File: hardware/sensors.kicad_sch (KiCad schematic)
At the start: 43 parts, among them U7 PCA9685PW

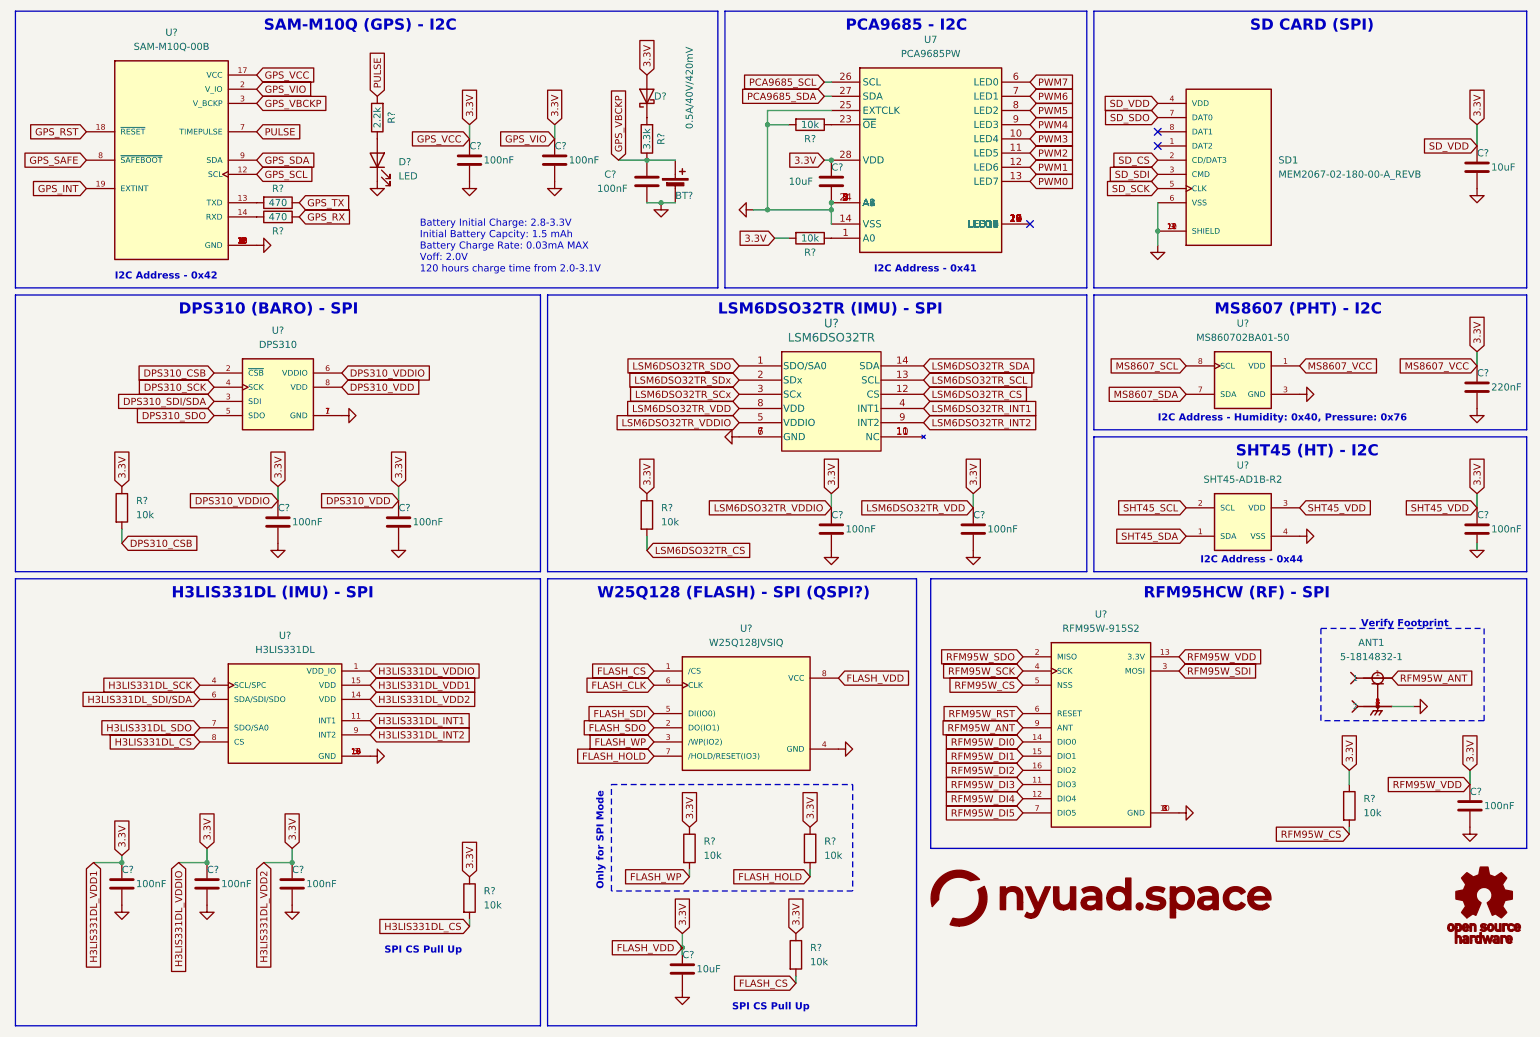
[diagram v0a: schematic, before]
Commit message: added BNO086
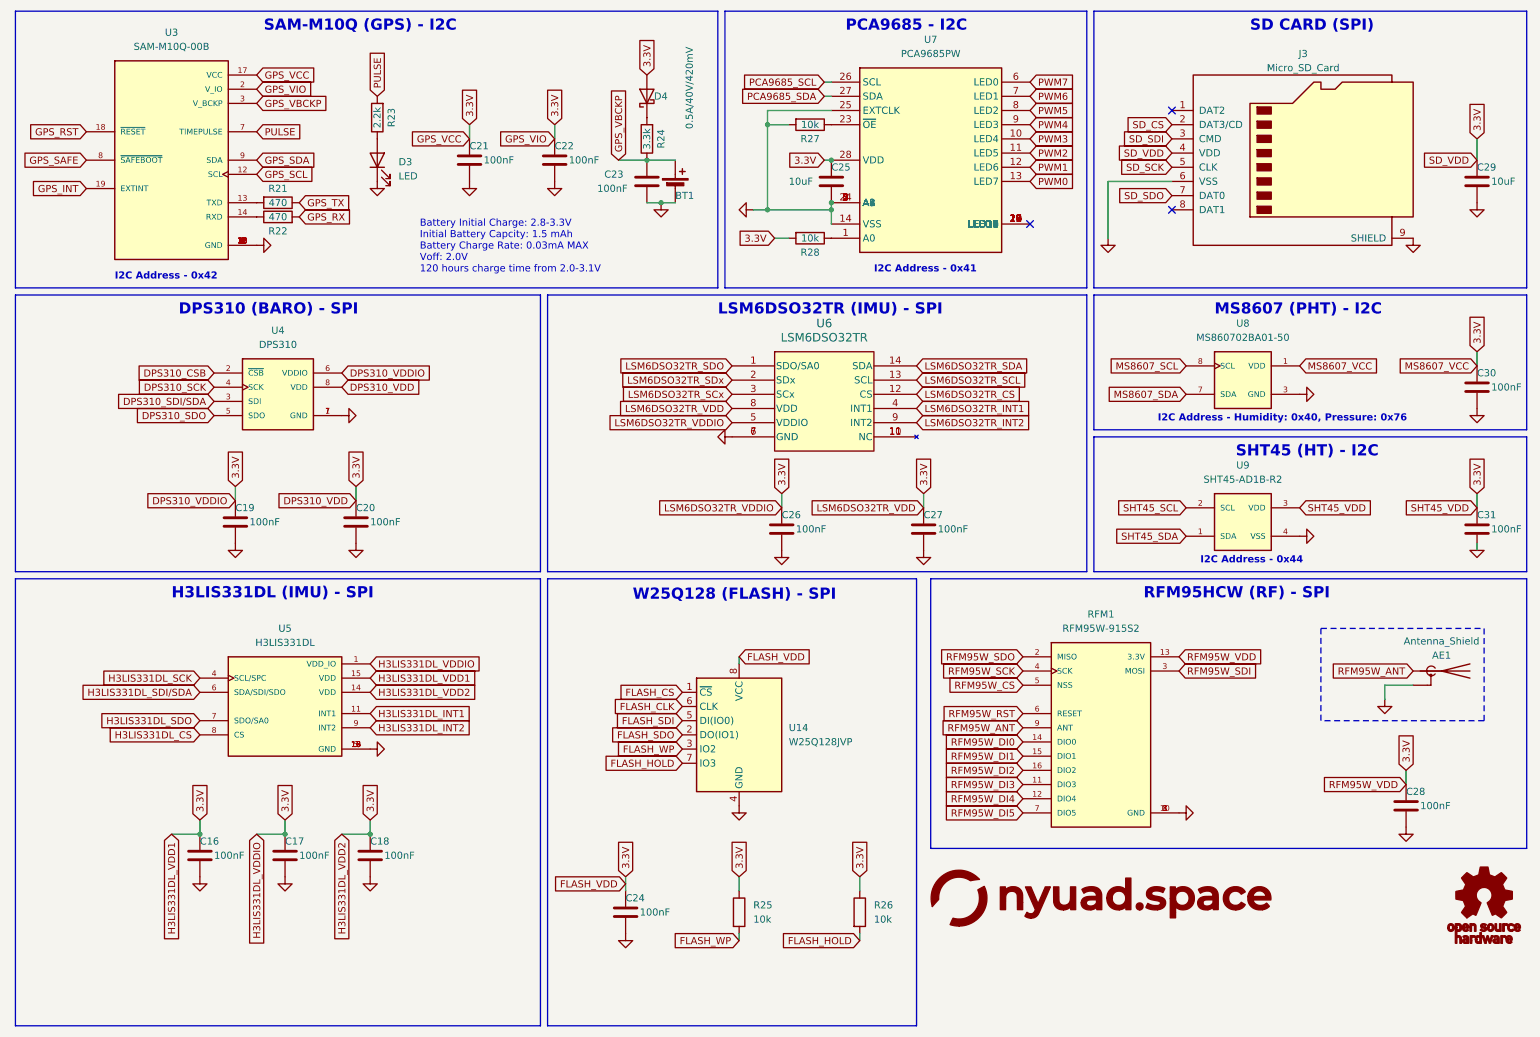
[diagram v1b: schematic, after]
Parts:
- removed ANT1: 5-1814832-1, 5-1814832-1:TE_5-1814832-1, symbol 5-1814832-1:5-1814832-1
- removed R? (x5): 10k, Resistor_SMD:R_0402_1005Metric, symbol Device:R
- removed SD1: MEM2067-02-180-00-A_REVB, MEM2067-02-180-00-A_REVB:GCT_MEM2067-02-180-00-A_REVB, symbol MEM2067-02-180-00-A_REVB:MEM2067-02-180-00-A_REVB
- removed U?: W25Q128JVSIQ, SOIC127P790X216-8N, symbol W25Q128JVSIQ:W25Q128JVSIQ
- added AE1: Antenna_Shield, 5-1814832-1:TE_5-1814832-1, symbol Device:Antenna_Shield
- added J3: Micro_SD_Card, symbol Connector:Micro_SD_Card
- added U14: W25Q128JVP, Package_SON:WSON-8-1EP_6x5mm_P1.27mm_EP3.4x4.3mm, symbol Memory_Flash:W25Q128JVP
- C24: renamed from C?; value 10uF -> 100nF; footprint Capacitor_SMD:C_0402_1005Metric -> (none)
- C25, C29: renamed from C?; footprint Capacitor_SMD:C_0603_1608Metric -> (none)
- C30: renamed from C?; value 220nF -> 100nF; footprint Capacitor_SMD:C_0603_1608Metric -> (none)
- D3: renamed from D?; footprint LED_SMD:LED_0402_1005Metric -> (none)
- D4: renamed from D?; footprint Diode_SMD:D_SOD-323 -> (none)
- R21, R22, R24, R27, R28: renamed from R?; footprint Resistor_SMD:R_0603_1608Metric -> (none)
- R23, R25, R26: renamed from R?; footprint Resistor_SMD:R_0402_1005Metric -> (none)
- RFM1: renamed from U?; footprint XCVR_RFM95W-915S2 -> (none)
- U3: renamed from U?; footprint XCVR_SAM-M10Q-00B -> (none)
- U4: renamed from U?; footprint XDCR_DPS310 -> (none)
- U5: renamed from U?; footprint QFN300X300X100-16N -> (none)
- U6: renamed from U?; footprint LGA-14L_2P5X3X0P83_STM -> (none)
- U7: footprint Package_SO:TSSOP-28_4.4x9.7mm_P0.65mm -> (none)
- U8: renamed from U?; footprint TE_MS860702BA01-50 -> (none)
- U9: renamed from U?; footprint SHT4X -> (none)
- gave numbers to parts that had none: 13
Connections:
- net 3.3V: now also J3.4 (VDD), U14.8 (VCC)
- net FLASH_CLK: now also U14.6 (CLK)
- net FLASH_CS: now also U14.1 (~{CS})
- net FLASH_HOLD: now also U14.7 (IO3)
- net FLASH_SDI: now also U14.5 (DI(IO0))
- net FLASH_SDO: now also U14.2 (DO(IO1))
- net FLASH_WP: now also U14.3 (IO2)
- net GND: now also AE1.2 (Shield), J3.6 (VSS), J3.9 (SHIELD), U14.4 (GND)
- net RFM95W_ANT: now also AE1.1 (A)
- net SD_CS: now also J3.2 (DAT3/CD)
- net SD_SCK: now also J3.5 (CLK)
- net SD_SDI: now also J3.3 (CMD)
- net SD_SDO: now also J3.7 (DAT0)
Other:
- note added: "W25Q128 (FLASH) - SPI"
- note removed: "Only for SPI Mode"
- note removed: "SPI CS Pull Up"
- note removed: "Verify Footprint"
- note removed: "W25Q128 (FLASH) - SPI (QSPI?)"
- moved on the sheet: C16, C17, C18, C19, C20, C24, C26, C27, C28, C29, R25, R26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

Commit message: rev2 component placement
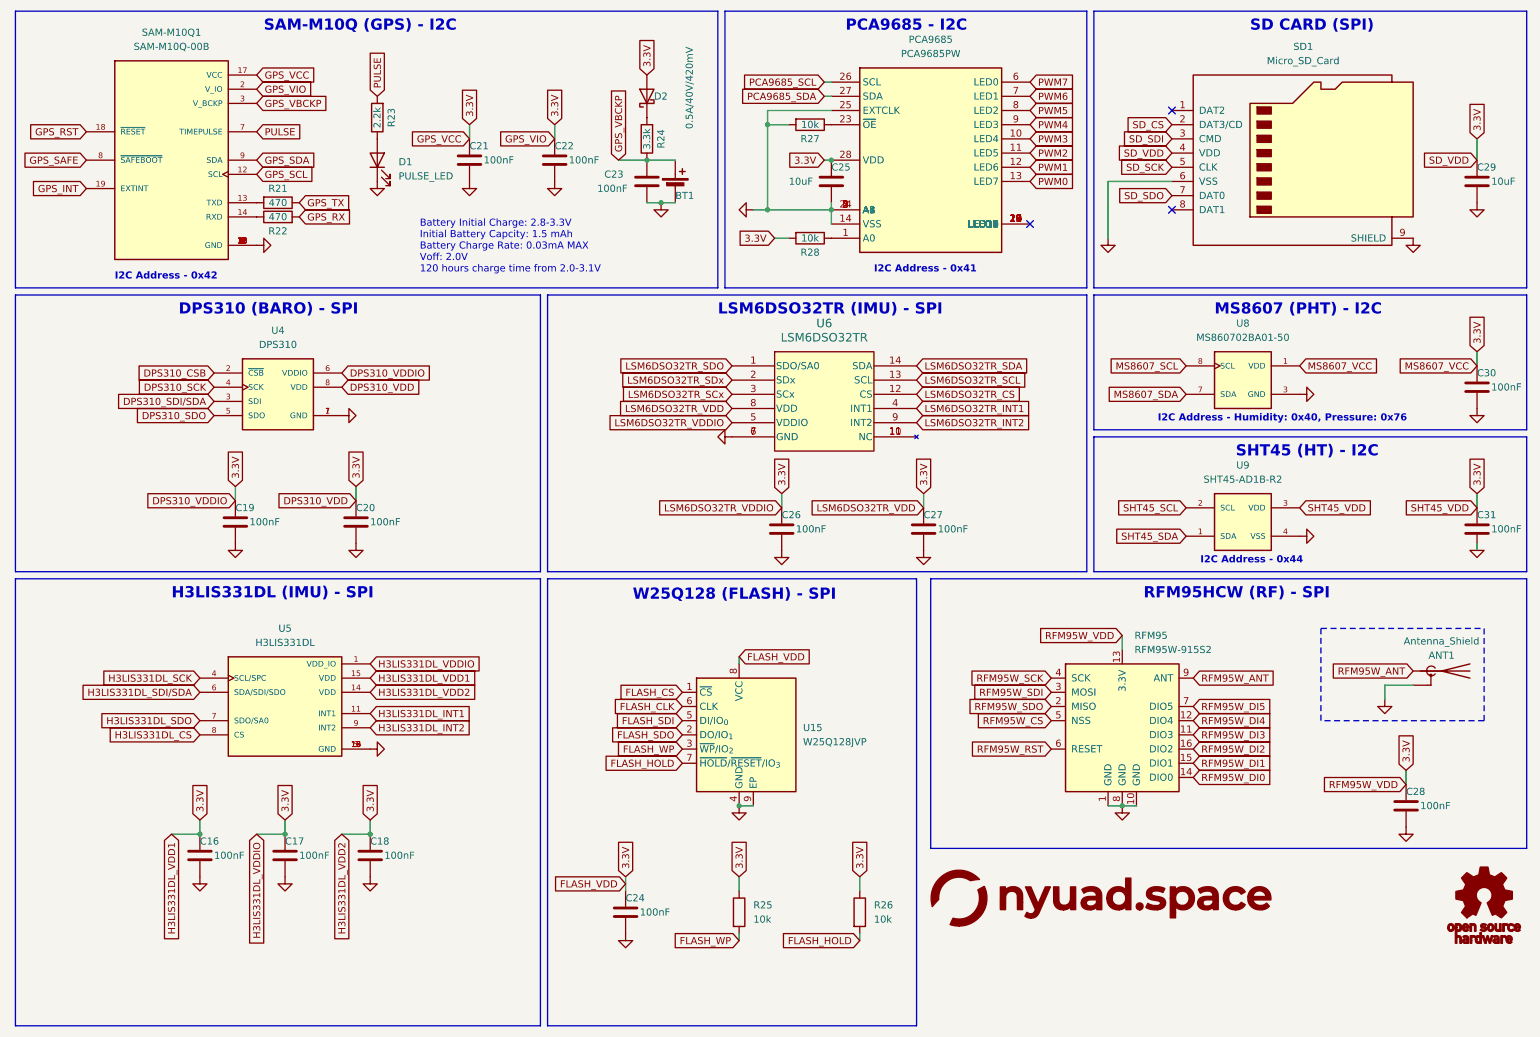
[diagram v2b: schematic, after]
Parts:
- removed RFM1: RFM95W-915S2, symbol RFM95W-915S2:RFM95W-915S2
- removed U14: W25Q128JVP, Package_SON:WSON-8-1EP_6x5mm_P1.27mm_EP3.4x4.3mm, symbol Memory_Flash:W25Q128JVP
- added RFM95: RFM95W-915S2, RF_Module:HOPERF_RFM9XW_SMD, symbol RF_Module:RFM95W-915S2
- added U15: W25Q128JVP, Package_SON:WSON-8-1EP_6x5mm_P1.27mm_EP3.4x4.3mm, symbol Memory_Flash:W25Q128JVP
- ANT1: renamed from AE1; footprint 5-1814832-1:TE_5-1814832-1 -> Connector_Coaxial:SMA_Amphenol_901-144_Vertical
- C24, C30: footprint (none) -> Capacitor_SMD:C_0402_1005Metric
- C25, C29: footprint (none) -> Capacitor_SMD:C_0805_2012Metric
- D1: renamed from D3; value LED -> PULSE_LED; footprint (none) -> LED_SMD:LED_0603_1608Metric
- D2: renamed from D4; footprint (none) -> Diode_SMD:D_SOD-323
- PCA9685: renamed from U7; footprint (none) -> Package_SO:TSSOP-28_4.4x9.7mm_P0.65mm
- R21, R22, R24, R25, R26, R27, R28: footprint (none) -> Resistor_SMD:R_0402_1005Metric
- R23: footprint (none) -> Resistor_SMD:R_0603_1608Metric
- SAM-M10Q1: renamed from U3; footprint (none) -> RF_GPS:ublox_SAM-M8Q
- SD1: renamed from J3; footprint (none) -> Connector_Card:microSD_HC_Wuerth_693072010801
- U4: footprint (none) -> DPS310:XDCR_DPS310
- U5: footprint (none) -> Package_LGA:LGA-16_3x3mm_P0.5mm_LayoutBorder3x5y
- U6: footprint (none) -> Package_LGA:LGA-14_3x2.5mm_P0.5mm_LayoutBorder3x4y
- U8: footprint (none) -> MS8607-02BA01:MS8607-02BA01
- U9: footprint (none) -> Sensor_Humidity:Sensirion_DFN-4_1.5x1.5mm_P0.8mm_SHT4x_NoCentralPad
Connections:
- net 3.3V: now also RFM95.13 (3.3V), U15.8 (VCC)
- net FLASH_CLK: now also U15.6 (CLK)
- net FLASH_CS: now also U15.1 (~{CS})
- net FLASH_HOLD: now also U15.7 (~{HOLD}/~{RESET}/IO_{3})
- net FLASH_SDI: now also U15.5 (DI/IO_{0})
- net FLASH_SDO: now also U15.2 (DO/IO_{1})
- net FLASH_WP: now also U15.3 (~{WP}/IO_{2})
- net GND: now also RFM95.1 (GND), RFM95.10 (GND), RFM95.8 (GND), U15.4 (GND), U15.9 (EP)
- net RFM95W_ANT: now also RFM95.9 (ANT)
- net RFM95W_CS: now also RFM95.5 (NSS)
- net RFM95W_DI0: now also RFM95.14 (DIO0)
- net RFM95W_DI1: now also RFM95.15 (DIO1)
- net RFM95W_DI2: now also RFM95.16 (DIO2)
- net RFM95W_DI3: now also RFM95.11 (DIO3)
- net RFM95W_DI4: now also RFM95.12 (DIO4)
- net RFM95W_DI5: now also RFM95.7 (DIO5)
- net RFM95W_RST: now also RFM95.6 (RESET)
- net RFM95W_SCK: now also RFM95.4 (SCK)
- net RFM95W_SDI: now also RFM95.3 (MOSI)
- net RFM95W_SDO: now also RFM95.2 (MISO)
